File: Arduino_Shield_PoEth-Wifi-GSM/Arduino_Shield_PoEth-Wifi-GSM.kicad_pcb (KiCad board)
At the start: 2 copper layers, 19 parts, among them U1 W5500

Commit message: Checking Eth PoE
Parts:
- removed C37, C38: 22uF_16V, Capacitor_THT:CP_Radial_D4.0mm_P1.50mm
- removed L1, L2: FerriteBead_0603_1.5A, PCM_4ms_Resistor:R_0603
- removed R10, R12, R9, RN8A1, RN8B1, RN8C1, RN8D1, RN9A1, RN9B1, RN9C1, RN9D1: 10K_0603, PCM_Resistor_SMD_AKL:R_0603_1608Metric
- removed R11, R15, R20: R_DNP, PCM_4ms_Resistor:R_0603
- removed U1: W5500, Package_QFP:LQFP-48_7x7mm_P0.5mm
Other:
- board outline added: 100 x 54 mm

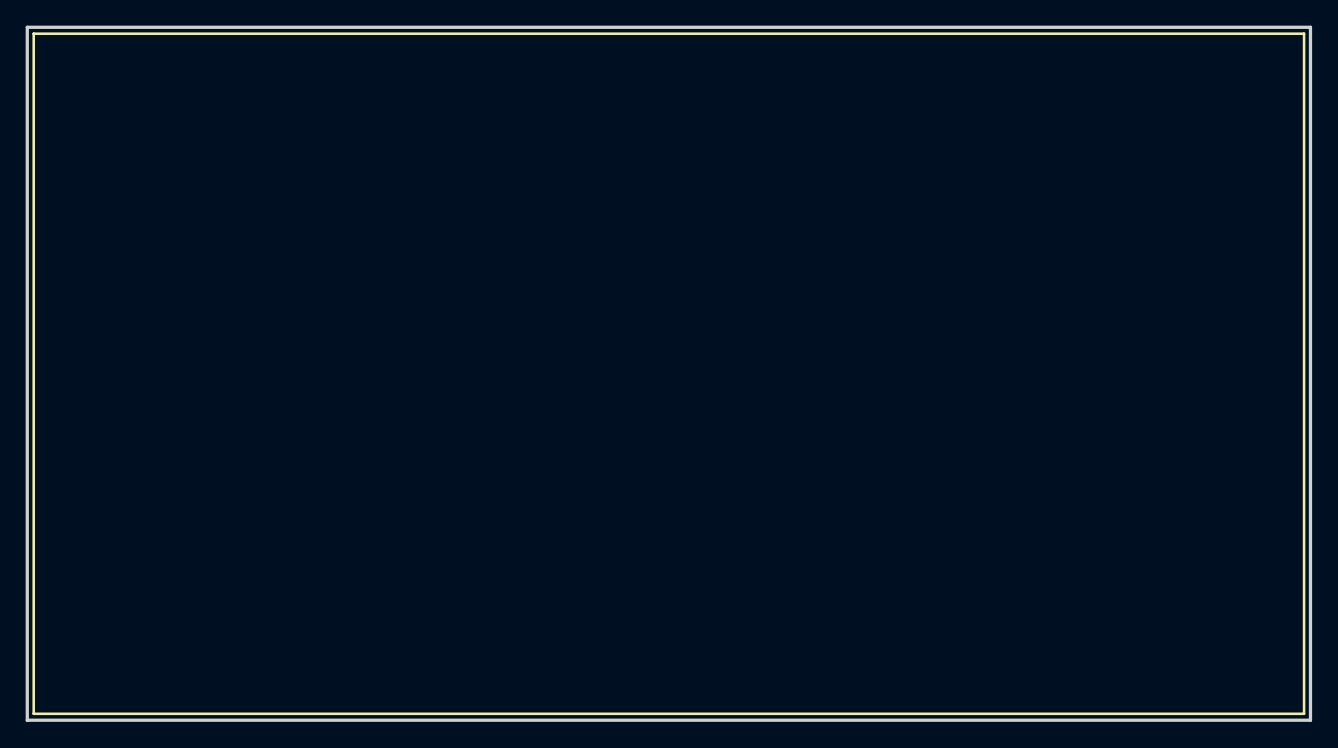
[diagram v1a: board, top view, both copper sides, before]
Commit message: Tuning serial and crystal tracks
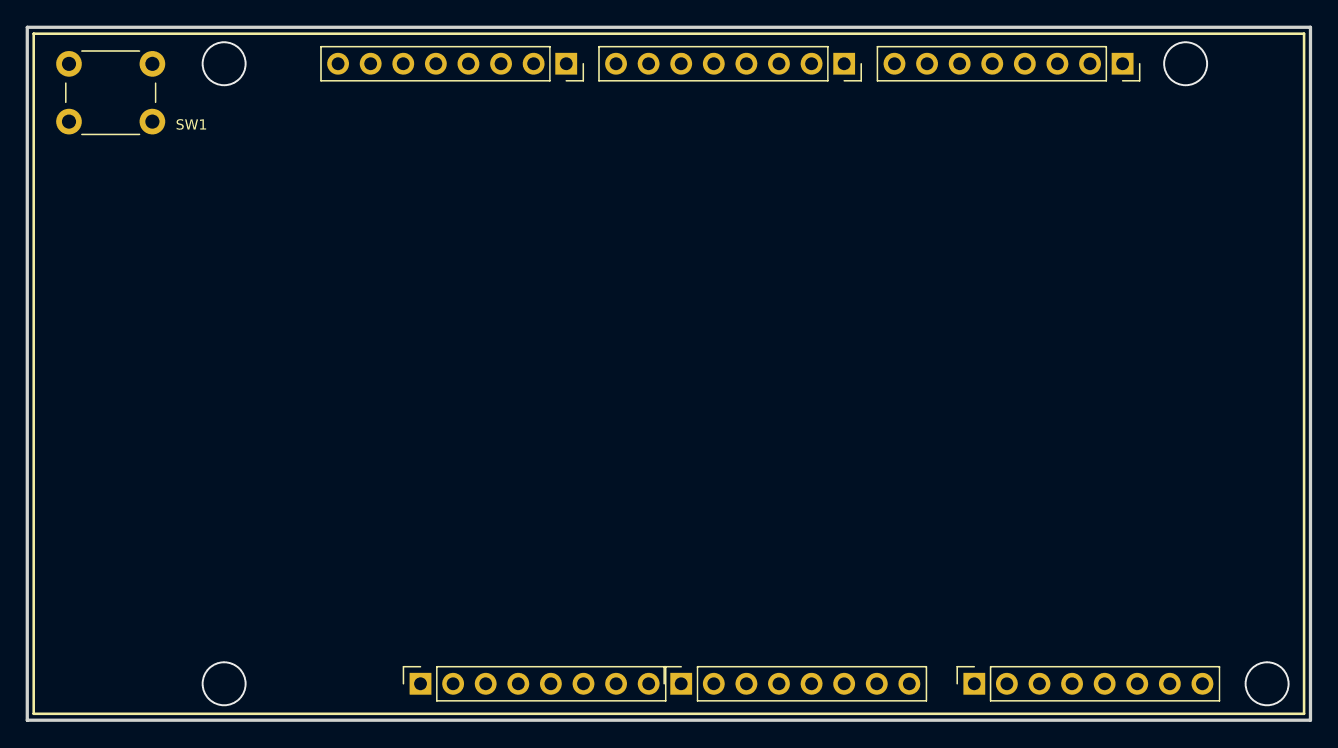
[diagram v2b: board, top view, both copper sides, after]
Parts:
- added ADC1: PINHD_1x8_Female, Connector_PinSocket_2.54mm:PinSocket_1x08_P2.54mm_Vertical, F.Cu at (92.2, 154.2)
- added ADC2: PINHD_1x8_Female, Connector_PinSocket_2.54mm:PinSocket_1x08_P2.54mm_Vertical, F.Cu at (115.0, 154.2)
- added COM1: PINHD_1x8_Female, Connector_PinSocket_2.54mm:PinSocket_1x08_P2.54mm_Vertical, F.Cu at (126.6, 105.8)
- added PWM1: PINHD_1x8_Female, Connector_PinSocket_2.54mm:PinSocket_1x08_P2.54mm_Vertical, F.Cu at (104.9, 105.8)
- added PWM2: PINHD_1x8_Female, Connector_PinSocket_2.54mm:PinSocket_1x08_P2.54mm_Vertical, F.Cu at (83.2, 105.8)
- added PWR1: PINHD_1x8_Female, Connector_PinSocket_2.54mm:PinSocket_1x08_P2.54mm_Vertical, F.Cu at (71.8, 154.2)
- added SW1: Push_Button, Button_Switch_THT:SW_PUSH_6mm, F.Cu at (44.5, 105.8)
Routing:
- net (no net): vias 0 -> 4

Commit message: Update Eth
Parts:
- added C1: 10nF_0603_16V, PCM_4ms_Capacitor:C_0603, F.Cu at (147.9, 136.4)
- added C10: 1nF 2KV 1206, PCM_4ms_Capacitor:C_1206, F.Cu at (161.2, 149.2)
- added C12: 100nF_0603_16V, PCM_4ms_Capacitor:C_0603, F.Cu at (56.4, 171.9)
- added C13: 100nF_0603_16V, PCM_4ms_Capacitor:C_0603, F.Cu at (56.4, 174.5)
- added C16: 22nF_0603_16V, PCM_4ms_Capacitor:C_0603, F.Cu at (147.9, 139.0)
- added C17: 6.8nF_0603_16V, PCM_4ms_Capacitor:C_0603, F.Cu at (147.9, 141.7)
- added C18: 6.8nF_0603_16V, PCM_4ms_Capacitor:C_0603, F.Cu at (147.9, 144.3)
- added C19: 10nF_0603_16V, PCM_4ms_Capacitor:C_0603, F.Cu at (147.9, 147.0)
- added C20: 10uF_25V, Capacitor_THT:CP_Radial_D5.0mm_P2.00mm, F.Cu at (180.0, 140.3)
- added C21: 0.1uF_0603_16V, PCM_4ms_Capacitor:C_0603, F.Cu at (147.9, 149.6)
- added C24: 0.1uF_0603_16V, PCM_4ms_Capacitor:C_0603, F.Cu at (152.1, 136.4)
- added C25: 0.1uF_0603_16V, PCM_4ms_Capacitor:C_0603, F.Cu at (152.1, 139.0)
- added C28: 0.1uF_0603_16V, PCM_4ms_Capacitor:C_0603, F.Cu at (152.1, 141.7)
- added C29: 0.1uF_0603_16V, PCM_4ms_Capacitor:C_0603, F.Cu at (152.1, 144.3)
- added C30: 0.1uF_0603_16V, PCM_4ms_Capacitor:C_0603, F.Cu at (152.1, 147.0)
- added C31: 10uF_25V, Capacitor_THT:CP_Radial_D5.0mm_P2.00mm, F.Cu at (180.0, 146.8)
- added C32: 0.1uF_0603_16V, PCM_4ms_Capacitor:C_0603, F.Cu at (152.1, 149.6)
- added C33: 18pF_0603_16V, PCM_4ms_Capacitor:C_0603, F.Cu at (156.4, 136.4)
- added C34: 18pF_0603_16V, PCM_4ms_Capacitor:C_0603, F.Cu at (156.4, 139.0)
- added C35: 4.7uF_0603_16V, PCM_4ms_Capacitor:C_0603, F.Cu at (156.4, 141.7)
- added C36: 0.1uF_0603_16V, PCM_4ms_Capacitor:C_0603, F.Cu at (156.4, 144.3)
- added Cp2: 47uF_10V, Capacitor_THT:CP_Radial_D4.0mm_P1.50mm, F.Cu at (65.5, 163.7)
- added J1: Conn_02x08, Connector_PinSocket_2.54mm:PinSocket_2x08_P2.54mm_Vertical, F.Cu at (136.1, 146.4)
- added J1: PINHD_2x4_Male, Connector_PinHeader_2.54mm:PinHeader_2x04_P2.54mm_Vertical, F.Cu at (160.8, 137.4)
- added J2: Conn_02x08, Connector_PinSocket_2.54mm:PinSocket_2x08_P2.54mm_Vertical, F.Cu at (136.1, 126.1)
- added J3: PINHD_1x2_Female, Connector_PinSocket_2.54mm:PinSocket_1x02_P2.54mm_Vertical, F.Cu at (136.1, 105.8)
- added J4: PINHD_1x2_Female, Connector_PinSocket_2.54mm:PinSocket_1x02_P2.54mm_Vertical, F.Cu at (136.1, 148.9)
- added L1: MH2029-300Y, FerriteBead_MH2029-300Y_Bourns:IND_BOURNS_MH2029, F.Cu at (181.7, 132.0)
- added LED_PB7: Yellow 0805, LED_SMD:LED_0805_2012Metric, F.Cu at (52.1, 172.1)
- added ON1: Green 0805, LED_SMD:LED_0805_2012Metric, F.Cu at (52.1, 175.1)
- added R24: 22R_0603, PCM_Resistor_SMD_AKL:R_0603_1608Metric, F.Cu at (168.4, 129.1)
- added R25: 10R_0603, PCM_Resistor_SMD_AKL:R_0603_1608Metric, F.Cu at (172.5, 112.8)
- added R4: 49R9_0603, PCM_Resistor_SMD_AKL:R_0603_1608Metric, F.Cu at (168.4, 112.8)
- added R45: 1M_0603, PCM_Resistor_SMD_AKL:R_0603_1608Metric, F.Cu at (172.5, 115.5)
- added R46: 12.4K_0603, PCM_Resistor_SMD_AKL:R_0603_1608Metric, F.Cu at (172.5, 118.2)
- added R5: 49R9_0603, PCM_Resistor_SMD_AKL:R_0603_1608Metric, F.Cu at (168.4, 115.5)
- added R6: 49R9_0603, PCM_Resistor_SMD_AKL:R_0603_1608Metric, F.Cu at (168.4, 118.2)
- added R7: 49R9_0603, PCM_Resistor_SMD_AKL:R_0603_1608Metric, F.Cu at (168.4, 120.9)
- added R8: 330R_0603, PCM_Resistor_SMD_AKL:R_0603_1608Metric, F.Cu at (168.4, 123.6)
- added R9: 330R_0603, PCM_Resistor_SMD_AKL:R_0603_1608Metric, F.Cu at (168.4, 126.4)
- added RJ45: RJ45_Abracon_ARJP11A-MASA-B-A-EMU2, Connector_RJ:RJ45_Abracon_ARJP11A-MA_Horizontal, F.Cu at (58.0, 119.7)
- added RN11: 33R_0603, PCM_Resistor_SMD_AKL:R_0603_1608Metric, F.Cu at (172.5, 120.9)
- added RN12: 33R_0603, PCM_Resistor_SMD_AKL:R_0603_1608Metric, F.Cu at (172.5, 123.6)
- added RN13: 33R_0603, PCM_Resistor_SMD_AKL:R_0603_1608Metric, F.Cu at (172.5, 126.4)
- added RN14: 33R_0603, PCM_Resistor_SMD_AKL:R_0603_1608Metric, F.Cu at (172.5, 129.1)
- added RN21: 10K_0603, PCM_Resistor_SMD_AKL:R_0603_1608Metric, F.Cu at (176.6, 112.8)
- added RN22: 10K_0603, PCM_Resistor_SMD_AKL:R_0603_1608Metric, F.Cu at (176.6, 115.5)
- added RN23: 10K_0603, PCM_Resistor_SMD_AKL:R_0603_1608Metric, F.Cu at (176.6, 118.2)
- added RN24: 10K_0603, PCM_Resistor_SMD_AKL:R_0603_1608Metric, F.Cu at (176.6, 120.9)
- added RN31: 10K_0603, PCM_Resistor_SMD_AKL:R_0603_1608Metric, F.Cu at (176.6, 123.6)
- added RN32: 10K_0603, PCM_Resistor_SMD_AKL:R_0603_1608Metric, F.Cu at (176.6, 126.4)
- added RN33: 10K_0603, PCM_Resistor_SMD_AKL:R_0603_1608Metric, F.Cu at (176.6, 129.1)
- added RN34: 10K_0603, PCM_Resistor_SMD_AKL:R_0603_1608Metric, F.Cu at (180.7, 112.8)
- added RN35: 1K_0603, PCM_Resistor_SMD_AKL:R_0603_1608Metric, F.Cu at (61.4, 162.2)
- added RN36: 1K_0603, PCM_Resistor_SMD_AKL:R_0603_1608Metric, F.Cu at (61.4, 165.0)
- added RN41: 10K_0603, PCM_Resistor_SMD_AKL:R_0603_1608Metric, F.Cu at (180.7, 115.5)
- added RN42: 10K_0603, PCM_Resistor_SMD_AKL:R_0603_1608Metric, F.Cu at (180.7, 118.2)
- added RN44: 10K_0603, PCM_Resistor_SMD_AKL:R_0603_1608Metric, F.Cu at (180.7, 120.9)
- added RN53: 10K_0603, PCM_Resistor_SMD_AKL:R_0603_1608Metric, F.Cu at (61.4, 167.7)
- added RN54: 10K_0603, PCM_Resistor_SMD_AKL:R_0603_1608Metric, F.Cu at (61.4, 170.4)
- added T1: PMV48XP_215, MOSFET_PMV48XP,215_Nexperia:TO-236_SOT23_NEX, F.Cu at (56.6, 178.3)
- added U1: W5500, Package_QFP:LQFP-48_7x7mm_P0.5mm, F.Cu at (87.5, 125.1)
- added U2: ATECC508A-SSHDA, Package_SO:SOIC-8_3.9x4.9mm_P1.27mm, F.Cu at (190.5, 147.7)
- added U3: LMV358IDGK, PCM_Package_SO_AKL:MSOP-8_3x3mm_P0.65mm, F.Cu at (63.1, 174.1)
- added UP1: LD1117S50CTR, LDO_LD1117S50CTR_STMicroelectronics:SOT-223_STM, F.Cu at (54.7, 147.3)
- added UP2: LP2985-3.3, Package_TO_SOT_SMD:SOT-23-5, F.Cu at (66.0, 168.8)
- added X2: 25MHz 18pF, Crystal_25MHz_AbraconLLC:XTAL_HC49P488W46L1150T500H350, F.Cu at (172.8, 133.7)
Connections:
- net AREF renamed /AREF
- PWM1 pad 1: RXD0 -> unconnected-(PWM1-Pad1)
- PWM1 pad 2: TXD0 -> unconnected-(PWM1-Pad2)
- PWM1 pad 3: Net-(U1-PE4) -> unconnected-(PWM1-Pad3)
- PWM1 pad 4: Net-(U1-PE5) -> unconnected-(PWM1-Pad4)
- PWM1 pad 6: Net-(U1-PE3) -> unconnected-(PWM1-Pad6)
- PWM2 pad 3: /PB4 -> unconnected-(PWM2-Pad3)
- PWM2 pad 4: /PB5 -> unconnected-(PWM2-Pad4)
- PWM2 pad 5: /PB6 -> unconnected-(PWM2-Pad5)
- PWM2 pad 6: /PB7 -> unconnected-(PWM2-Pad6)
- PWM2 pad 7: GND -> unconnected-(PWM2-Pad7)
- PWR1 pad 3: RESET1 -> /RESET1
- PWR1 pad 8: VIN -> +12V
- SW1 pad 1: (no net) -> /RESET1
- SW1 pad 2: (no net) -> GND
